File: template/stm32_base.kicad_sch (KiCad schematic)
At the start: 41 parts, among them J1 Network Connector, J2 B2B STLink connector, SW1 SW_Push, U1 LD39050PU33R, U2 STM32G474RBT6, U3 SN65HVD230, Y1 8MHz

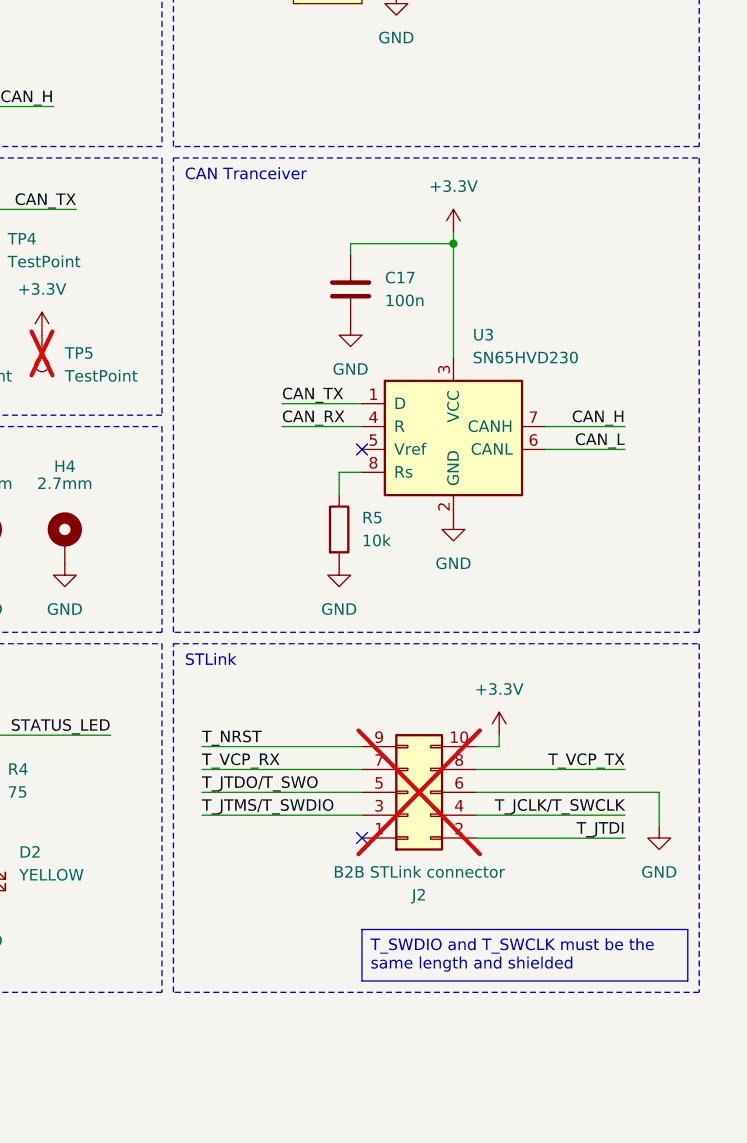
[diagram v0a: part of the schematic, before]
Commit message: Change B2B connector to STDC14 connector
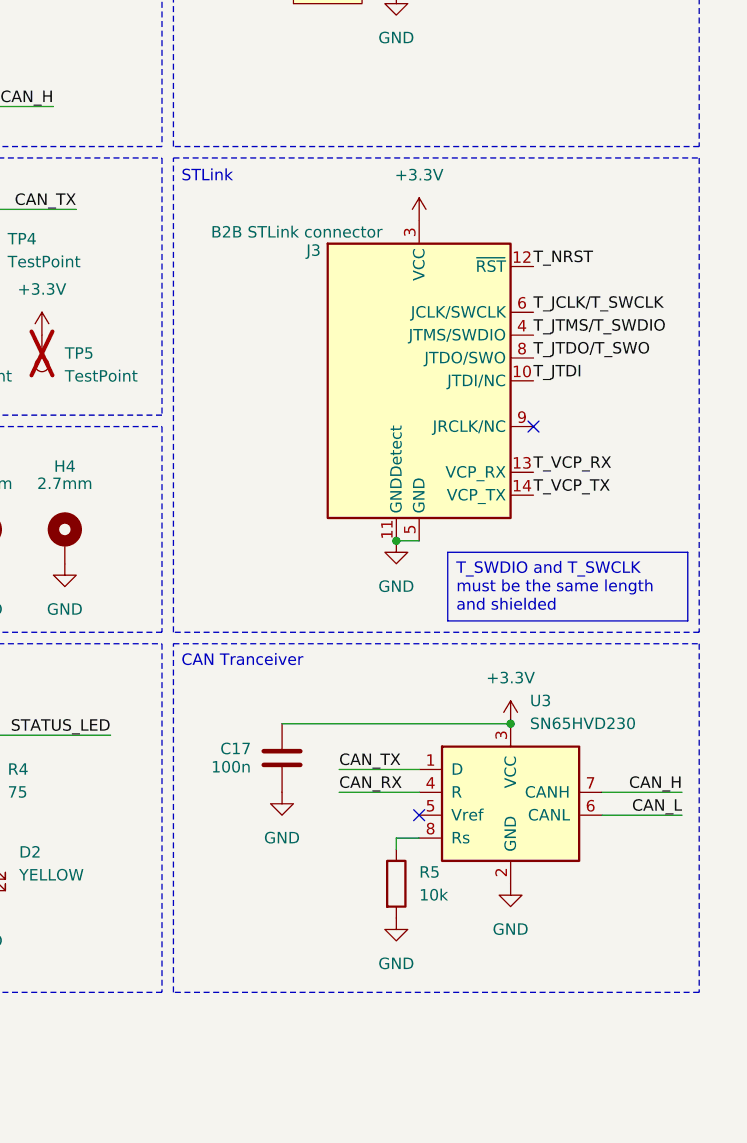
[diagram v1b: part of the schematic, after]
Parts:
- removed J2: B2B STLink connector, Exocet:AVX 00-9159-010-BTB Connector, symbol Connector_Generic:Conn_02x05_Odd_Even
- added J3: B2B STLink connector, Connector_PinHeader_1.27mm:PinHeader_2x07_P1.27mm_Vertical_SMD, symbol Connector:Conn_ST_STDC14
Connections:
- net +3.3V: now also J3.3 (VCC)
- net GND: now also J3.11 (GNDDetect), J3.5 (GND), J3.7 (GND)
- net T_JCLK/T_SWCLK: now also J3.6 (JCLK/SWCLK)
- net T_JTDI: now also J3.10 (JTDI/NC)
- net T_JTDO/T_SWO: now also J3.8 (JTDO/SWO)
- net T_JTMS/T_SWDIO: now also J3.4 (JTMS/SWDIO)
- net T_NRST: now also J3.12 (~{RST})
- net T_VCP_RX: now also J3.13 (VCP_RX)
- net T_VCP_TX: now also J3.14 (VCP_TX)
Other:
- moved on the sheet: C17, R5, U3

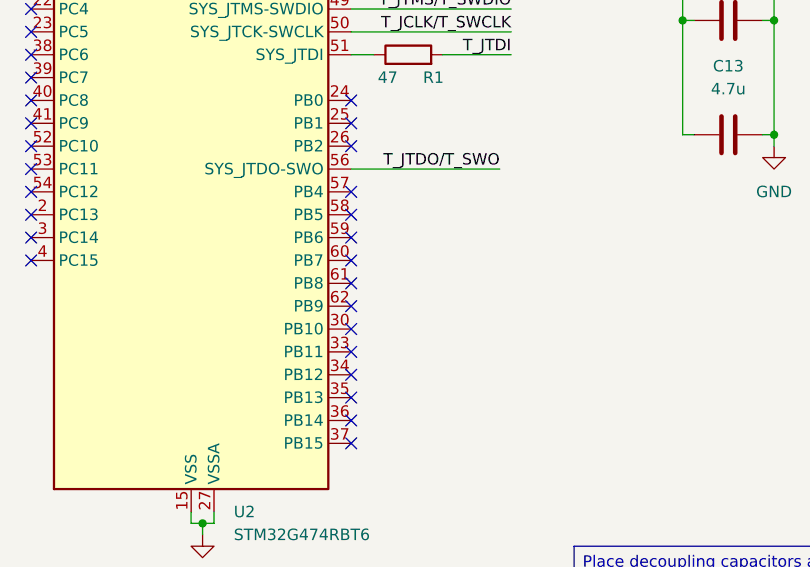
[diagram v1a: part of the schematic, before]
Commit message: Connect BOOT0 to GND through 10k resistor
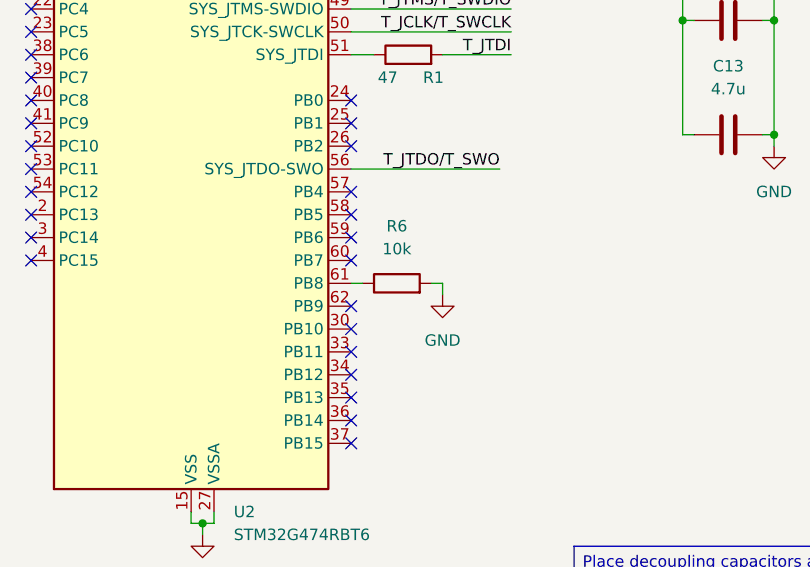
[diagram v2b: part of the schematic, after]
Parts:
- added R6: 10k, Resistor_SMD:R_0603_1608Metric, symbol Device:R
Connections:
- net GND: now also R6.2
- net at U2.61 (PB8): now also R6.1
- no-connect marks 43 -> 42
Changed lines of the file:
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@@
 	)
 	(no_connect
-		(at 99.06 158.75)
-	)
-	(no_connect
 		(at 99.06 166.37)
 	)
@@
 	(wire
 		(pts
+			(xy 107.95 158.75) (xy 109.22 158.75)
+		)
+		(stroke
+			(width 0)
+			(type default)
+		)
+	)
+	(wire
+		(pts
 			(xy 135.89 76.2) (xy 135.89 91.44)
 		)
@@
 	(wire
 		(pts
+			(xy 100.33 158.75) (xy 99.06 158.75)
+		)
+		(stroke
+			(width 0)
+			(type default)
+		)
+	)
+	(wire
+		(pts
 			(xy 194.31 25.4) (xy 196.85 25.4)
 		)
@@
 	(wire
 		(pts
+			(xy 109.22 158.75) (xy 109.22 160.02)
+		)
+		(stroke
+			(width 0)
+			(type default)
+		)
+	)
+	(wire
+		(pts
 			(xy 243.84 132.08) (xy 252.73 132.08)
 		)
@@
 	)
 	(symbol
+		(lib_id "Device:R")
+		(at 104.14 158.75 90)
+		(unit 1)
+		(exclude_from_sim no)
+		(in_bom yes)
+		(on_board yes)
+		(dnp no)
+		(fields_autoplaced yes)
+		(property "Reference" "R6"
+			(at 104.14 152.4 90)
+			(effects
+				(font
+					(size 1.27 1.27)
+				)
+			)
+		)
+		(property "Value" "10k"
+			(at 104.14 154.94 90)
+			(effects
+				(font
+					(size 1.27 1.27)
+				)
+			)
+		)
+		(property "Footprint" "Resistor_SMD:R_0603_1608Metric"
+			(at 104.14 160.528 90)
+			(effects
+				(font
+					(size 1.27 1.27)
+				)
+				(hide yes)
+			)
+		)
+		(property "Datasheet" "~"
+			(at 104.14 158.75 0)
+			(effects
+				(font
+					(size 1.27 1.27)
+				)
+				(hide yes)
+			)
+		)
+		(property "Description" "Resistor"
+			(at 104.14 158.75 0)
+			(effects
+				(font
+					(size 1.27 1.27)
+				)
+				(hide yes)
+			)
+		)
+		(property "JLCPCB" "C25804"
+			(at 104.14 158.75 0)
+			(effects
+				(font
+					(size 1.27 1.27)
+				)
+				(hide yes)
+			)
+		)
+		(pin "1"
+		)
+		(pin "2"
+		)
+		(instances
+			(project "template"
+				(path "/4b4cf3aa-c94c-4150-b9c5-35049cd71136/7d59fd70-1fff-4c9c-ae77-583b08aef567"
+					(reference "R6")
+					(unit 1)
+				)
+			)
+		)
+	)
+	(symbol
 		(lib_id "Device:C")
 		(at 140.97 142.24 90)
@@
 					(unit 1)
 				)
+			)
+		)
+	)
+	(symbol
+		(lib_id "power:GND")
+		(at 109.22 160.02 0)
+		(unit 1)
+		(exclude_from_sim no)
+		(in_bom yes)
+		(on_board yes)
+		(dnp no)
+		(fields_autoplaced yes)
+		(property "Reference" "#PWR031"
+			(at 109.22 166.37 0)
+			(effects
+				(font
+					(size 1.27 1.27)
+				)
+				(hide yes)
+			)
+		)
+		(property "Value" "GND"
+			(at 109.22 165.1 0)
+			(effects
+				(font
+					(size 1.27 1.27)
+				)
+			)
+		)
+		(property "Footprint" ""
+			(at 109.22 160.02 0)
+			(effects
+				(font
+					(size 1.27 1.27)
+				)
+				(hide yes)
+			)
+		)
+		(property "Datasheet" ""
+			(at 109.22 160.02 0)
+			(effects
+				(font
+					(size 1.27 1.27)
+				)
+				(hide yes)
+			)
+		)
+		(property "Description" "Power symbol creates a global label with name \"GND\" , ground"
+			(at 109.22 160.02 0)
+			(effects
+				(font
+					(size 1.27 1.27)
+				)
+				(hide yes)
+			)
+		)
+		(pin "1"
+		)
+		(instances
+			(project ""
+				(path "/4b4cf3aa-c94c-4150-b9c5-35049cd71136/7d59fd70-1fff-4c9c-ae77-583b08aef567"
+					(reference "#PWR031")
+					(unit 1)
+				)

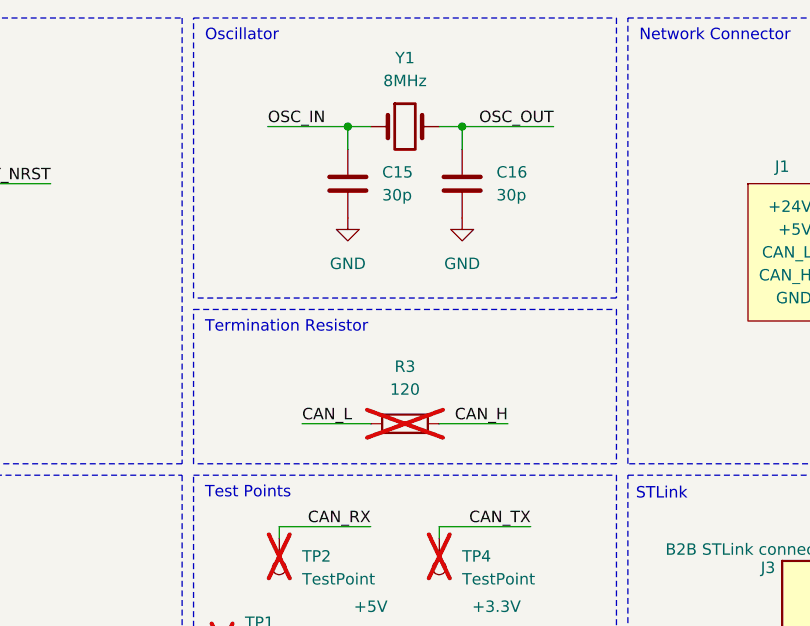
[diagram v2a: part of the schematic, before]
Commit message: Remove Termination Resistor (CAN Network)
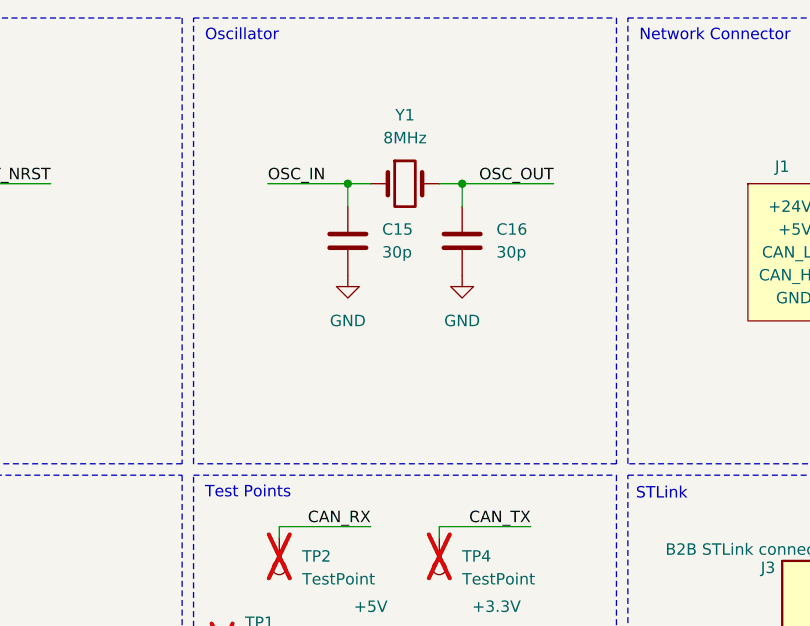
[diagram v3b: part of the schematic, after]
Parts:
- removed R3: 120, Resistor_THT:R_Axial_DIN0309_L9.0mm_D3.2mm_P12.70mm_Horizontal, symbol Device:R
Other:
- note removed: "Termination Resistor"
- moved on the sheet: C15, C16, Y1
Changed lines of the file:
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@@
 	(rectangle
 		(start 177.165 13.335)
-		(end 224.155 44.45)
+		(end 224.155 62.865)
 		(stroke
 			(width 0)
@@
 	)
 	(rectangle
-		(start 177.165 45.72)
-		(end 224.155 62.865)
-		(stroke
-			(width 0)
-			(type dash)
-		)
-		(fill
-			(type none)
-		)
-	)
-	(rectangle
 		(start 177.165 93.98)
 		(end 224.155 116.84)
@@
 		)
 	)
-	(text "Termination Resistor"
-		(exclude_from_sim no)
-		(at 178.435 46.99 0)
-		(effects
-			(font
-				(size 1.27 1.27)
-			)
-			(justify left top)
-		)
-	)
 	(text "Oscillator"
 		(exclude_from_sim no)
@@
 	)
 	(junction
-		(at 194.31 25.4)
+		(at 194.31 31.75)
 		(diameter 0)
 		(color 0 0 0 0)
@@
 	)
 	(junction
-		(at 207.01 25.4)
+		(at 207.01 31.75)
 		(diameter 0)
 		(color 0 0 0 0)
@@
 	(wire
 		(pts
-			(xy 194.31 25.4) (xy 196.85 25.4)
+			(xy 194.31 31.75) (xy 196.85 31.75)
 		)
 		(stroke
@@
 	(wire
 		(pts
-			(xy 185.42 25.4) (xy 194.31 25.4)
+			(xy 185.42 31.75) (xy 194.31 31.75)
 		)
 		(stroke
@@
 	(wire
 		(pts
-			(xy 207.01 25.4) (xy 207.01 27.94)
+			(xy 207.01 31.75) (xy 207.01 34.29)
 		)
 		(stroke
@@
 	(wire
 		(pts
-			(xy 217.17 25.4) (xy 207.01 25.4)
+			(xy 217.17 31.75) (xy 207.01 31.75)
 		)
 		(stroke
@@
 	(wire
 		(pts
-			(xy 204.47 58.42) (xy 212.09 58.42)
-		)
-		(stroke
-			(width 0)
-			(type default)
-		)
-	)
-	(wire
-		(pts
 			(xy 135.89 104.14) (xy 137.16 104.14)
 		)
@@
 	(wire
 		(pts
-			(xy 194.31 27.94) (xy 194.31 25.4)
+			(xy 194.31 34.29) (xy 194.31 31.75)
 		)
 		(stroke
@@
 	(wire
 		(pts
-			(xy 204.47 25.4) (xy 207.01 25.4)
+			(xy 204.47 31.75) (xy 207.01 31.75)
 		)
 		(stroke
@@
 	(wire
 		(pts
-			(xy 189.23 58.42) (xy 196.85 58.42)
-		)
-		(stroke
-			(width 0)
-			(type default)
-		)
-	)
-	(wire
-		(pts
 			(xy 140.97 45.72) (xy 139.7 45.72)
 		)
@@
 		)
 	)
-	(label "CAN_L"
-		(at 189.23 58.42 0)
-		(effects
-			(font
-				(size 1.27 1.27)
-			)
-			(justify left bottom)
-		)
-	)
 	(label "T_JTDI"
 		(at 265.43 88.9 0)
@@
 	)
 	(label "OSC_IN"
-		(at 185.42 25.4 0)
+		(at 185.42 31.75 0)
 		(effects
 			(font
@@
 		)
 	)
-	(label "CAN_H"
-		(at 212.09 58.42 180)
-		(effects
-			(font
-				(size 1.27 1.27)
-			)
-			(justify right bottom)
-		)
-	)
 	(label "CAN_RX"
 		(at 243.84 134.62 0)
@@
 	)
 	(label "OSC_OUT"
-		(at 217.17 25.4 180)
+		(at 217.17 31.75 180)
 		(effects
 			(font
@@
 	(symbol
 		(lib_id "power:GND")
-		(at 194.31 35.56 0)
+		(at 194.31 41.91 0)
 		(unit 1)
 		(exclude_from_sim no)
@@
 		(fields_autoplaced yes)
 		(property "Reference" "#PWR017"
-			(at 194.31 41.91 0)
+			(at 194.31 48.26 0)
 			(effects
 				(font
@@
 		)
 		(property "Value" "GND"
-			(at 194.31 40.64 0)
+			(at 194.31 46.99 0)
 			(effects
 				(font
@@
 		)
 		(property "Footprint" ""
-			(at 194.31 35.56 0)
+			(at 194.31 41.91 0)
 			(effects
 				(font
@@
 		)
 		(property "Datasheet" ""
-			(at 194.31 35.56 0)
+			(at 194.31 41.91 0)
 			(effects
 				(font
@@
 		)
 		(property "Description" "Power symbol creates a global label with name \"GND\" , ground"
-			(at 194.31 35.56 0)
+			(at 194.31 41.91 0)
 			(effects
 				(font
@@
 	(symbol
 		(lib_id "power:GND")
-		(at 207.01 35.56 0)
+		(at 207.01 41.91 0)
 		(unit 1)
 		(exclude_from_sim no)
@@
 		(fields_autoplaced yes)
 		(property "Reference" "#PWR022"
-			(at 207.01 41.91 0)
+			(at 207.01 48.26 0)
 			(effects
 				(font
@@
 		)
 		(property "Value" "GND"
-			(at 207.01 40.64 0)
+			(at 207.01 46.99 0)
 			(effects
 				(font
@@
 		)
 		(property "Footprint" ""
-			(at 207.01 35.56 0)
+			(at 207.01 41.91 0)
 			(effects
 				(font
@@
 		)
 		(property "Datasheet" ""
-			(at 207.01 35.56 0)
+			(at 207.01 41.91 0)
 			(effects
 				(font
@@
 		)
 		(property "Description" "Power symbol creates a global label with name \"GND\" , ground"
-			(at 207.01 35.56 0)
+			(at 207.01 41.91 0)
 			(effects
 				(font
@@
 	(symbol
 		(lib_id "Device:C")
-		(at 194.31 31.75 0)
+		(at 194.31 38.1 0)
 		(unit 1)
 		(exclude_from_sim no)
@@
 		(fields_autoplaced yes)
 		(property "Reference" "C15"
-			(at 198.12 30.4799 0)
+			(at 198.12 36.8299 0)
 			(effects
 				(font
@@
 		)
 		(property "Value" "30p"
-			(at 198.12 33.0199 0)
+			(at 198.12 39.3699 0)
 			(effects
 				(font
@@
 		)
 		(property "Footprint" "Capacitor_SMD:C_0603_1608Metric"
-			(at 195.2752 35.56 0)
+			(at 195.2752 41.91 0)
 			(effects
 				(font
@@
 		)
 		(property "Datasheet" "~"
-			(at 194.31 31.75 0)
+			(at 194.31 38.1 0)
 			(effects
 				(font
@@
 		)
 		(property "Description" "Unpolarized capacitor"
-			(at 194.31 31.75 0)
+			(at 194.31 38.1 0)
 			(effects
 				(font
@@
 		)
 		(property "JLCPCB" "C1658"
-			(at 194.31 31.75 0)
+			(at 194.31 38.1 0)
 			(effects
 				(font
@@
 	(symbol
 		(lib_id "Exocet:HSE_Oscillator")
-		(at 200.66 25.4 0)
+		(at 200.66 31.75 0)
 		(unit 1)
 		(exclude_from_sim no)
@@
 		(fields_autoplaced yes)
 		(property "Reference" "Y1"
-			(at 200.66 17.78 0)
+			(at 200.66 24.13 0)
 			(effects
 				(font
@@
 		)
 		(property "Value" "8MHz"
-			(at 200.66 20.32 0)
+			(at 200.66 26.67 0)
 			(effects
 				(font
@@
 		)
 		(property "Footprint" "Exocet:Crystal_SMD_HC49-SD"
-			(at 200.66 25.4 0)
+			(at 200.66 31.75 0)
 			(effects
 				(font
@@
 		)
 		(property "Datasheet" "~"
-			(at 200.66 25.4 0)
+			(at 200.66 31.75 0)
 			(effects
 				(font
@@
 		)
 		(property "Description" "Two pin crystal"
-			(at 200.66 25.4 0)
+			(at 200.66 31.75 0)
 			(effects
 				(font
@@
 		)
 		(property "JLCPCB" "C12674"
-			(at 200.66 25.4 0)
+			(at 200.66 31.75 0)
 			(effects
 				(font
@@
 		)
 		(property "Part Name" "X49SM8MSD2SC"
-			(at 200.66 25.4 0)
+			(at 200.66 31.75 0)
 			(effects
 				(font
@@
 	)
 	(symbol
-		(lib_id "Device:R")
-		(at 200.66 58.42 90)
-		(unit 1)
-		(exclude_from_sim no)
-		(in_bom yes)
-		(on_board yes)
-		(dnp yes)
-		(fields_autoplaced yes)
-		(property "Reference" "R3"
-			(at 200.66 52.07 90)
-			(effects
-				(font
-					(size 1.27 1.27)
-				)
-			)
-		)
-		(property "Value" "120"
-			(at 200.66 54.61 90)
-			(effects
-				(font
-					(size 1.27 1.27)
-				)
-			)
-		)
-		(property "Footprint" "Resistor_THT:R_Axial_DIN0309_L9.0mm_D3.2mm_P12.70mm_Horizontal"
-			(at 200.66 60.198 90)
-			(effects
-				(font
-					(size 1.27 1.27)
-				)
-				(hide yes)
-			)
-		)
-		(property "Datasheet" "~"
-			(at 200.66 58.42 0)
-			(effects
-				(font
-					(size 1.27 1.27)
-				)
-				(hide yes)
-			)
-		)
-		(property "Description" "Resistor"
-			(at 200.66 58.42 0)
-			(effects
-				(font
-					(size 1.27 1.27)
-				)
-				(hide yes)
-			)
-		)
-		(pin "1"
-		)
-		(pin "2"
-		)
-		(instances
-			(project "template"
-				(path "/4b4cf3aa-c94c-4150-b9c5-35049cd71136/7d59fd70-1fff-4c9c-ae77-583b08aef567"
-					(reference "R3")
-					(unit 1)
-				)
-			)
-		)
-	)
-	(symbol
 		(lib_id "Device:C")
 		(at 140.97 116.84 90)
@@
 	(symbol
 		(lib_id "Device:C")
-		(at 207.01 31.75 0)
+		(at 207.01 38.1 0)
 		(unit 1)
 		(exclude_from_sim no)
@@
 		(fields_autoplaced yes)
 		(property "Reference" "C16"
-			(at 210.82 30.4799 0)
+			(at 210.82 36.8299 0)
 			(effects
 				(font
@@
 		)
 		(property "Value" "30p"
-			(at 210.82 33.0199 0)
+			(at 210.82 39.3699 0)
 			(effects
 				(font
@@
 		)
 		(property "Footprint" "Capacitor_SMD:C_0603_1608Metric"
-			(at 207.9752 35.56 0)
+			(at 207.9752 41.91 0)
 			(effects
 				(font
@@
 		)
 		(property "Datasheet" "~"
-			(at 207.01 31.75 0)
+			(at 207.01 38.1 0)
 			(effects
 				(font
@@
 		)
 		(property "Description" "Unpolarized capacitor"
-			(at 207.01 31.75 0)
+			(at 207.01 38.1 0)
 			(effects
 				(font
@@
 		)
 		(property "JLCPCB" "C1658"
-			(at 207.01 31.75 0)
+			(at 207.01 38.1 0)
 			(effects
 				(font

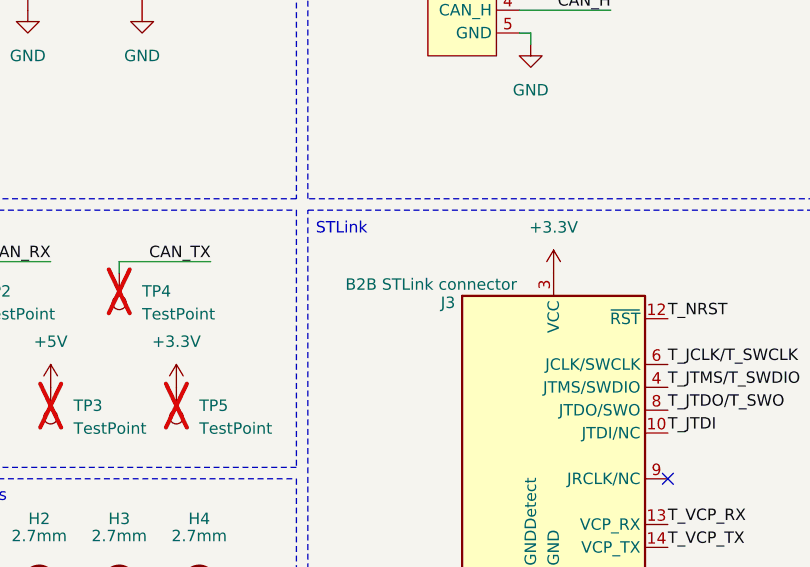
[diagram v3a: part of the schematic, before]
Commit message: Assing JLCPCB Part Number
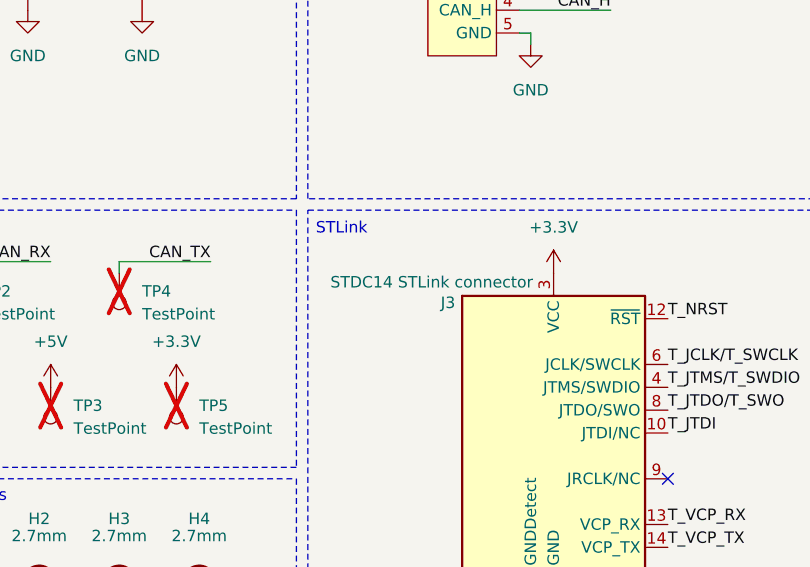
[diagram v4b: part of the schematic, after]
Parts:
- J3: value B2B STLink connector -> STDC14 STLink connector; JLCPCB (none) -> C7465995
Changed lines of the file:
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@@
 			)
 		)
-		(property "Value" "B2B STLink connector"
-			(at 248.666 72.39 0)
+		(property "Value" "STDC14 STLink connector"
+			(at 250.444 72.136 0)
 			(effects
 				(font
@@
 			(at 252.73 88.9 0)
 			(effects
+				(font
+					(size 1.27 1.27)
+				)
+				(hide yes)
+			)
+		)
+		(property "JLCPCB" "C7465995"
+			(at 252.73 88.9 0)
+			(effects
